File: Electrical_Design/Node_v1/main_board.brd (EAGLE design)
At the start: 101.6 x 100 mm, 88 parts, among them IC1 TP4056, IC2 REG1117, IC3 DS18B20U+, U2 ESP-WROOM-32, U3 BME280, U4 CCS811

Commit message: restored backup save file
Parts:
- moved R21 139.3 mm to (59.9, 94.2)
- moved R18 137.2 mm to (80.8, 34.3)
- moved C8 133.8 mm to (47.8, 94.5)
- moved R20 133.3 mm to (60.5, 89.2)
- moved R17 130.8 mm to (79.8, 38.4)
- moved C7 129.6 mm to (53.6, 85.9)
- moved C6 129.2 mm to (54.4, 96.0)
- moved R16 124.0 mm to (78.2, 43.4)
- moved R19 122.8 mm to (53.8, 90.7)
- moved R15 118.4 mm to (77.7, 47.0)
- moved C1 113.8 mm to (74.4, 35.1)
- moved R3 112.3 mm to (65.3, 43.2)
- moved R2 107.2 mm to (65.3, 39.1)
- moved C10 106.3 mm to (72.6, 44.2)
- moved R1 101.7 mm to (66.0, 36.1), turned to 180 degrees
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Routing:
- net N$15: track 0.00 -> 58.0 mm, vias 0 -> 1
- net SCL: track 0.00 -> 51.2 mm, vias 0 -> 1
- net SDA: track 0.00 -> 45.4 mm, vias 0 -> 1
- net N$14: track 0.00 -> 43.5 mm, vias 0 -> 2
- net N$16: track 0.00 -> 42.2 mm
- net N$17: track 0.00 -> 39.0 mm
- net N$45: track 6.78 -> 17.6 mm, vias 0 -> 1
- net N$18: track 73.7 -> 84.4 mm, vias 1 -> 3
- net N$39: track 4.11 -> 14.0 mm, vias 0 -> 1
- net N$44: track 7.14 -> 13.4 mm, vias 0 -> 1
- net N$22: track 46.9 -> 46.2 mm, vias 0 -> 1

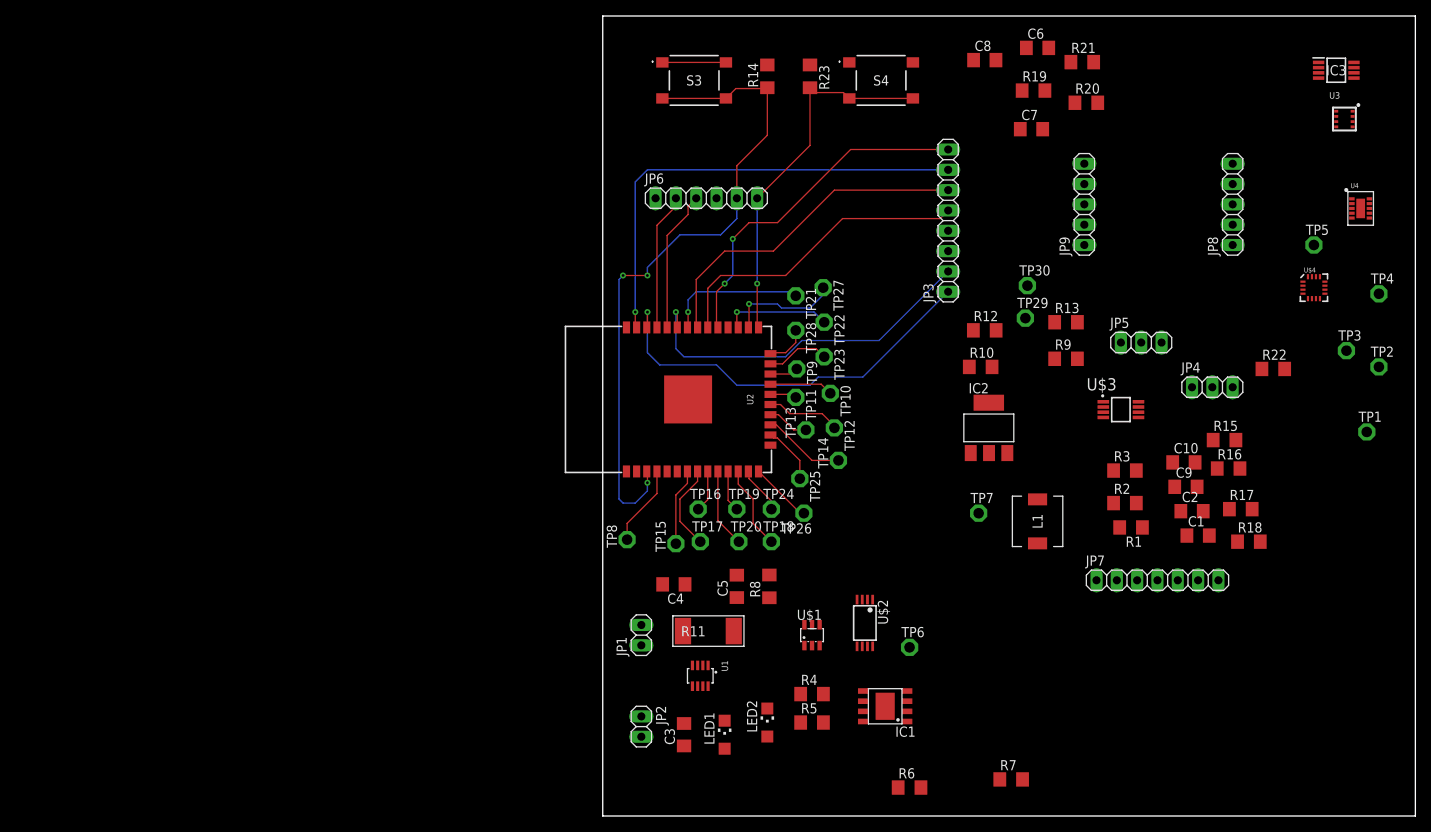
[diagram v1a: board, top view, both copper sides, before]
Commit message: Completes main board layout -- outstanding - isolate planes from divider line - remove planes from under esp antenna - generatre drc report
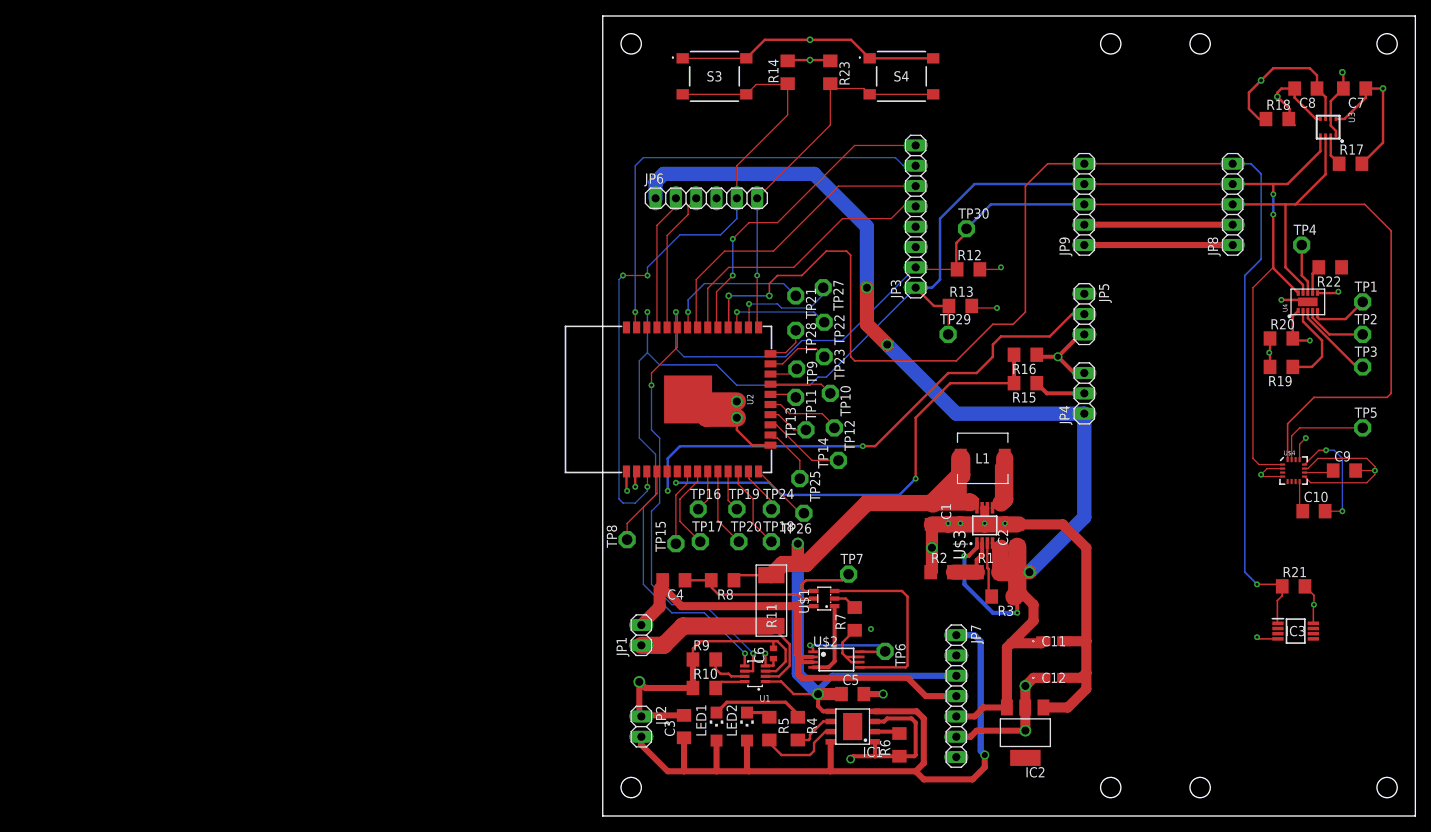
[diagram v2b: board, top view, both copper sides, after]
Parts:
- added C11, C12: T489A106K010ATA2K2, SamacSys_Parts:T489A
- C6: device adafruit:C1206 -> adafruit:R0402
- moved C6 82.6 mm to (21.3, 20.3), turned to 90 degrees
- moved R21 70.7 mm to (86.4, 28.7)
- moved IC3 70.3 mm to (86.6, 23.1)
- moved R9 58.8 mm to (12.7, 19.6)
- moved R10 53.0 mm to (12.7, 16.0)
- moved R18 53.0 mm to (84.3, 87.1)
- moved R19 46.4 mm to (84.8, 56.1), turned to 180 degrees
- moved R17 45.3 mm to (93.5, 81.5)
- moved C7 40.7 mm to (94.0, 90.9), turned to 180 degrees
- moved C8 40.3 mm to (87.9, 90.9), turned to 180 degrees
- moved IC2 38.4 mm to (52.8, 10.4), turned to 180 degrees
- moved R20 38.2 mm to (84.8, 59.7)
- moved C1 33.4 mm to (41.1, 37.8), turned to 270 degrees
- moved R16 29.1 mm to (52.8, 57.7), turned to 180 degrees
- moved JP7 29.0 mm to (44.2, 15.0), turned to 270 degrees
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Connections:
- removed net GND1: JP7.4
- removed net VCC: JP7.1, JP7.2, JP7.3
- new net N$60: R9.2, U1.7
- new net N$61: R10.2, U1.8
- new net SOLAR-: JP7.2
- net +3V3: now also C12.1; no longer R10.2, R9.2, U1.7, U1.8
- net +5V: now also C11.1
- net BATT+: now also JP7.3
- net BATT-: now also JP7.4
- net GND: now also C11.2, C12.2
- net SOLAR+: now also JP7.1
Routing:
- net GND: track 7.95 -> 274.6 mm, vias 0 -> 20
- net SDA: track 45.4 -> 223.5 mm, vias 1 -> 3
- net GPIO17: track 0.00 -> 167.8 mm, vias 0 -> 3
- net +5V: track 0.00 -> 161.6 mm, vias 0 -> 5
- net SCL: track 51.2 -> 212.7 mm, vias 1 -> 4
- net +3V3: track 0.00 -> 112.2 mm, vias 0 -> 14
- net BATT+: track 0.00 -> 107.6 mm, vias 0 -> 2
- net SOLAR+: track 0.00 -> 94.9 mm, vias 0 -> 1
- net N$21: track 0.00 -> 64.5 mm, vias 0 -> 2
- net BATT-: track 0.00 -> 60.3 mm
- net N$24: track 0.00 -> 56.7 mm, vias 0 -> 2
- net N$13: track 0.36 -> 26.7 mm
- net N$8: track 0.00 -> 24.1 mm
- net N$12: track 0.00 -> 17.7 mm
- net N$28: track 0.00 -> 14.6 mm, vias 0 -> 2
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- added copper zone on layer 2, net +3V3
- added copper zone on layer 15, net GND
- added copper zone on layer 15, net N$59

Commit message: Updates Schematics - adds BOM
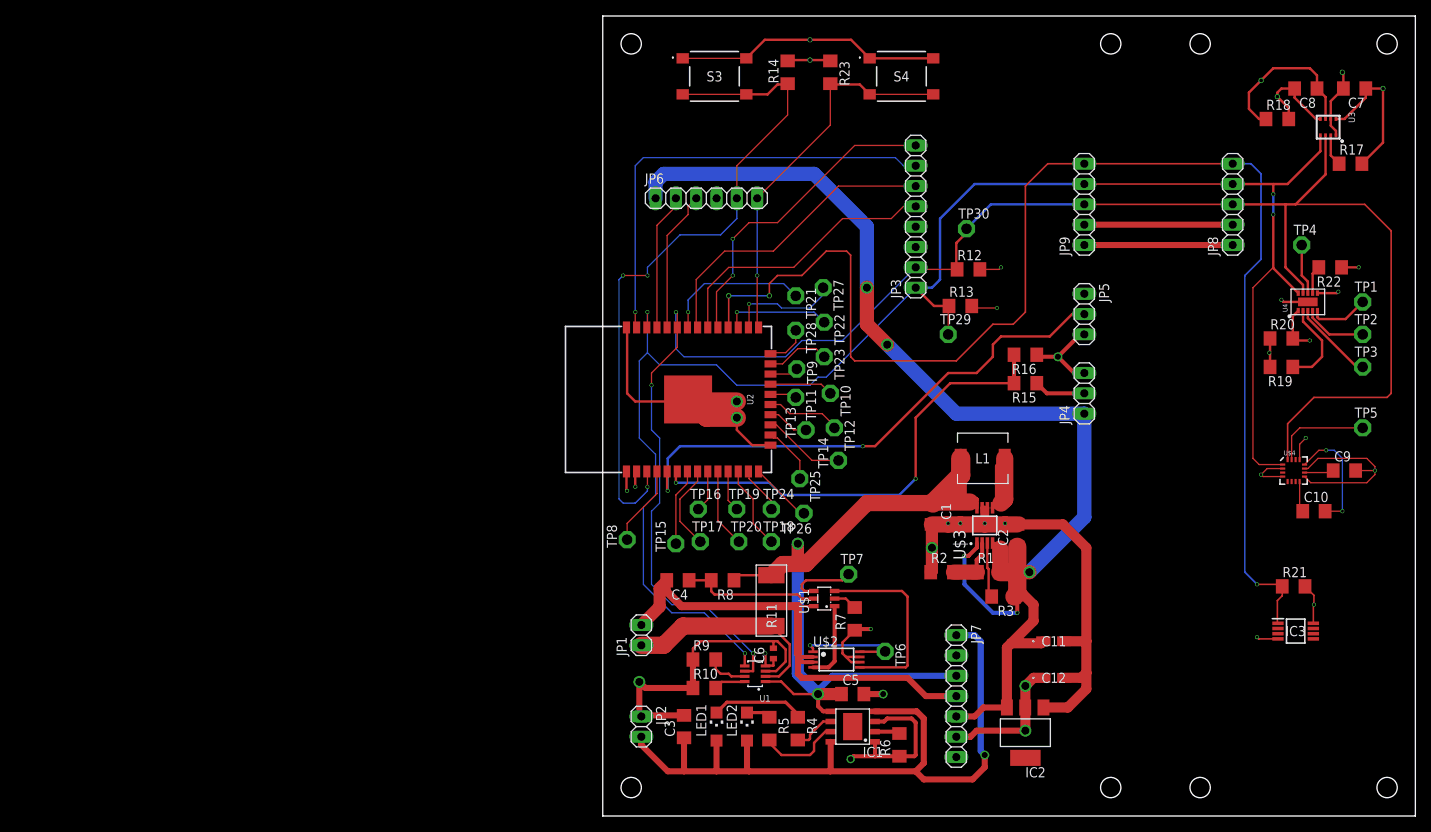
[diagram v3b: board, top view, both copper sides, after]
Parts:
- moved C4 0.51 mm to (9.40, 29.5)
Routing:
- net GND: track 274.6 -> 295.4 mm, vias 20 -> 21
- net +5V: track 161.6 -> 158.9 mm
- net N$21: track 64.5 -> 67.0 mm
- net N$24: track 56.7 -> 58.2 mm
- net BATT-: track 60.3 -> 61.4 mm
- net N$2: track 7.42 -> 6.91 mm
